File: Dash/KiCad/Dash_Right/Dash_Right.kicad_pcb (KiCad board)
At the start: 2 copper layers, 78.7 x 69.2 mm, 36 parts, among them J1 Conn_01x04, J2 Conn_01x03, J3 Conn_01x03, J5 Conn_02x03_Odd_Even, J6 Conn_01x04, J7 Conn_01x14, Q1 PSMN5R2-60YL, SW1 SW_SPDT, SW2 SW_SPDT, U1 ATmega328P-AU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

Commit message: first layout design
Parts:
- added G***: LOGO, AERO_CUSTOM:AERO_Logo_10x4mm, B.Cu at (183.9, 84.8)
- C4, R1, R2: moved to F.Cu
- C6, R9, U4: moved to B.Cu
- moved J5 42.3 mm to (201.9, 57.1), turned to 180 degrees
- moved H2 37.1 mm to (202.2, 97.1)
- moved Y1 19.7 mm to (181.1, 79.0), turned to 270 degrees
- moved U3 18.8 mm to (180.8, 73.3)
- moved U4 18.6 mm to (168.0, 87.9)
- moved R9 18.2 mm to (166.2, 97.0)
- moved U1 18.1 mm to (165.5, 73.9)
- moved R8 17.6 mm to (186.8, 66.2), turned to 0 degrees
- moved R4 15.6 mm to (149.2, 82.3)
- moved C5 14.8 mm to (182.9, 66.2), turned to 180 degrees
- moved C2 9.55 mm to (166.2, 80.3), turned to 0 degrees
- moved R2 7.52 mm to (163.6, 95.7)
- moved Q1 5.03 mm to (150.1, 90.0)
- moved R5 5.01 mm to (174.6, 62.9), turned to 0 degrees
- moved R7 4.74 mm to (191.6, 62.7), turned to 0 degrees
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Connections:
- J1 pad 2: /RTD_BTN -> /RTD_LED
- J1 pad 3: /RTD_LED -> /RTD_BTN
- J6 pad 1: GND -> +12V
- J6 pad 2: /CANL -> /CAN+
- J6 pad 3: /CANH -> /CAN-
- J6 pad 4: +12V -> GND
- J7 pad 1: +12V -> /RTD_IND_OUT
- J7 pad 10: /RTD_IND_OUT -> GND
- J7 pad 14: GND -> +12V
- J7 pad 2: +12V -> /CAN+
- J7 pad 3: /CANH -> /CAN-
- J7 pad 4: /CANH -> +5V
- J7 pad 5: /CANL -> +5V
- J7 pad 6: /CANL -> /CAN+
- J7 pad 7: +5V -> /CAN-
- J7 pad 9: +5V -> +12V
- R9 pad 1: /CANH -> /CAN+
- R9 pad 2: /CANL -> /CAN-
- U1 pad 10: /TMS_LED -> /IMD_LED
- U1 pad 11: /BMS_LED -> /TMS_LED
- U1 pad 12: /RTD_IND -> /RTD_BTN
- U1 pad 13: /RTD_BTN -> /RTD_LED
- U1 pad 14: /RTD_LED -> /RTD_IND
- U1 pad 2: /IMD_LED -> /BMS_LED
- U1 pad 25: /COOLING -> /DIRECTION
- U1 pad 26: /DIRECTION -> /COOLING
- U1 pad 32: (no net) -> /CAN_INT
- U3 pad 12: (no net) -> /CAN_INT
- U4 pad 6: /CANL -> /CAN-
- U4 pad 7: /CANH -> /CAN+
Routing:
- net +5V: track 0.00 -> 179.1 mm, vias 0 -> 3
- net /CAN-: track 0.00 -> 66.8 mm
- net /CAN+: track 0.00 -> 66.8 mm
- net +12V: track 0.00 -> 65.2 mm
- net /SCK: track 0.00 -> 56.4 mm, vias 0 -> 2
- net /MISO: track 0.00 -> 56.2 mm, vias 0 -> 2
- net /MOSI: track 0.00 -> 51.1 mm, vias 0 -> 2
- net /RESET: track 0.00 -> 38.6 mm, vias 0 -> 1
- net /COOLING: track 0.00 -> 36.8 mm
- net /REGEN: track 0.00 -> 35.2 mm, vias 0 -> 1
- net Net-(C3-Pad1): track 0.00 -> 34.8 mm
- net /COAST: track 0.00 -> 33.6 mm, vias 0 -> 1
- net /DIRECTION: track 0.00 -> 30.6 mm
- net /BMS_LED: track 0.00 -> 28.2 mm
- net /IMD_LED: track 0.00 -> 27.0 mm
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- added copper zone on F.Cu, net +5V
- added copper zone on F.Cu, net /RTD_IND_OUT
- added copper zone on B.Cu, net GND
- added copper zone on F.Cu, net GND

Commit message: update PCB Layout
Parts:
- removed G***: LOGO, AERO_CUSTOM:AERO_Logo_10x4mm
- J7: moved to B.Cu
- turned J7 to 180 degrees
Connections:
- J7 pad 1: /RTD_IND_OUT -> +5V
- J7 pad 10: GND -> +12V
- J7 pad 14: +12V -> GND
- J7 pad 2: /CAN+ -> +5V
- J7 pad 4: +5V -> /CAN+
- J7 pad 5: +5V -> /RTD_IND_OUT
- J7 pad 6: /CAN+ -> +12V
- J7 pad 7: /CAN- -> +5V
- J7 pad 8: +5V -> /CAN-
- J7 pad 9: +12V -> /CAN+

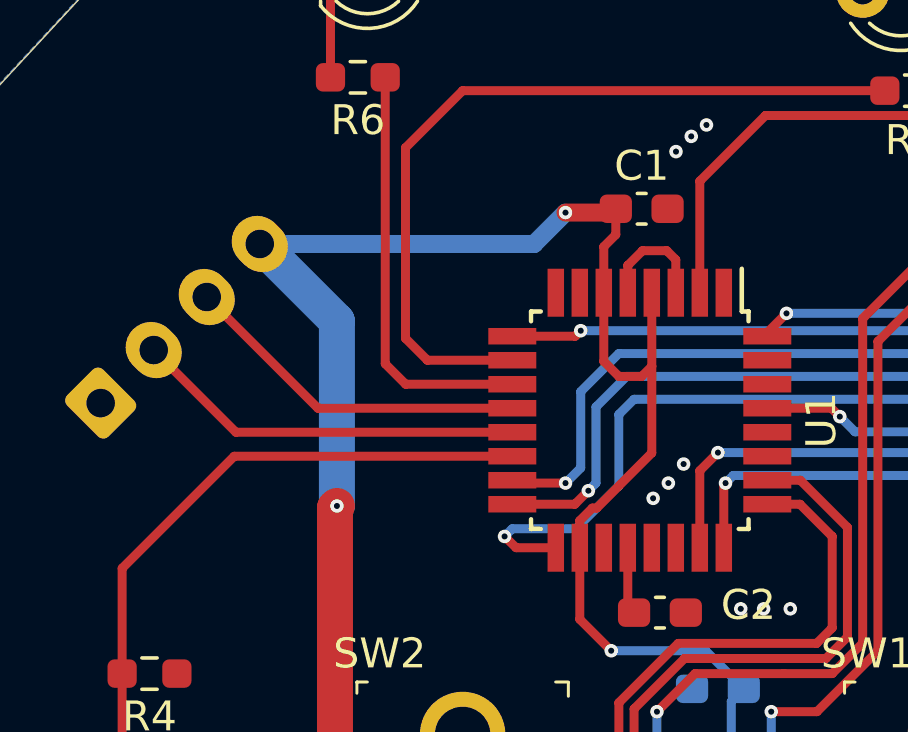
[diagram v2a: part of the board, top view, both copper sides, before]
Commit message: update start button pin
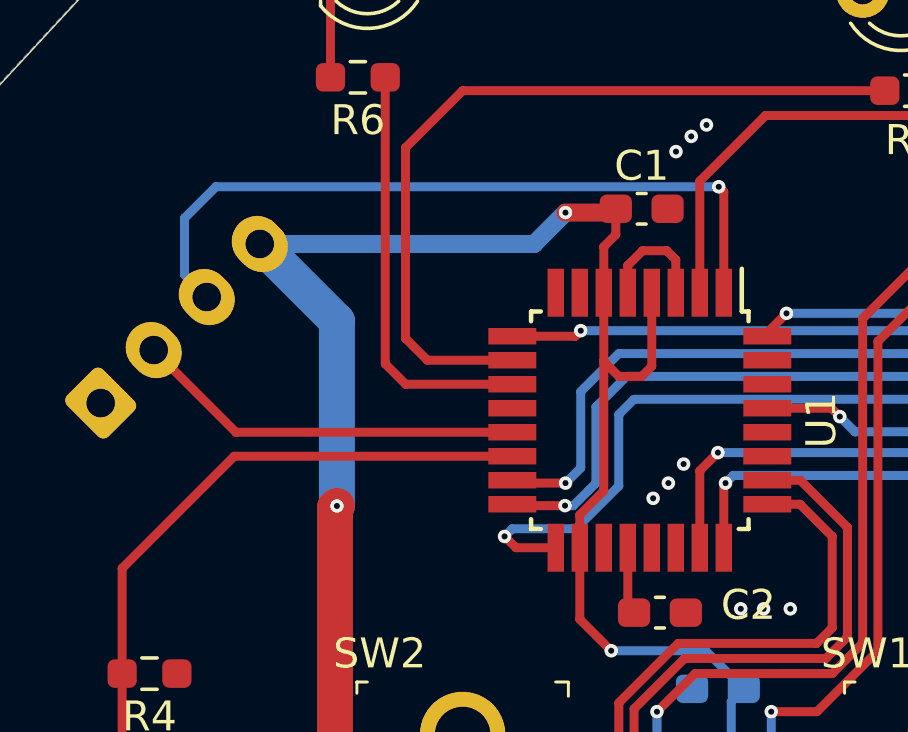
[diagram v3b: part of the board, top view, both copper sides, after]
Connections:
- U1 pad 1: (no net) -> /RTD_BTN
- U1 pad 12: /RTD_BTN -> (no net)
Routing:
- net /RTD_BTN: track 11.7 -> 25.5 mm, vias 0 -> 1
- net +5V: track 179.1 -> 178.5 mm

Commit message: gerber files
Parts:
- added G***: LOGO, AERO_CUSTOM:AERO_Logo_10x4mm, B.Cu at (184.8, 85.1)
